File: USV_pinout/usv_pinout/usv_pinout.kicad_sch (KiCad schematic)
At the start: 3 parts

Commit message: Mostly finish, missing jetson connections
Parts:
- added LM2596_Module1, LM2596_Module2: ~, symbol vanttec_pcbs_libs:LM2596_Module
- added X8R_telemetry: ~, symbol vanttec_pcbs_libs:X8R
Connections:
- net X8R_SBUS: now reaches STM32. (ESC_1)
- net X8R_SBUS: now also X8R_telemetry. (SBUS)
- new net ?+: LM2596_Module2. (OUT+)
- new net Barrel_Jack_GND: PDB2. (+)
- new net Barrel_Jack_VIN: PDB2. (+)
- new net LM2596_1+: LM2596_Module1. (OUT+), PDB2. (+)
- new net LM2596_1-: LM2596_Module1. (OUT+), PDB2. (+)
- new net LM2596_2+: LM2596_Module2. (OUT+), PDB2. (+)
- new net LM2596_2-: LM2596_Module2. (OUT+), PDB2. (+)
- new net X8R_GND: LM2596_Module1. (OUT+), STM32. (ESC_1), X8R_telemetry. (SBUS)
- new net X8R_VIN: LM2596_Module1. (OUT+), X8R_telemetry. (SBUS)
- no-connect marks 47 -> 55
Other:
- note added: "ESC1 and ESC2 == PWM ESC7 and ESC8 == PWM"
- note added: "FrSky X8R Operating V: 4-10V"
- note added: "Step-Down Regulators (LM2596)"
- note added: "huh"
- note removed: "IMPORTANTE: Falta de conectar: - Buck Converters - No se a que vaya uno de los bucks - Radio? (O la neta no se que sea) - Las conexiones de la Jetson la neta no creo que importen"
- moved on the sheet: PDB2

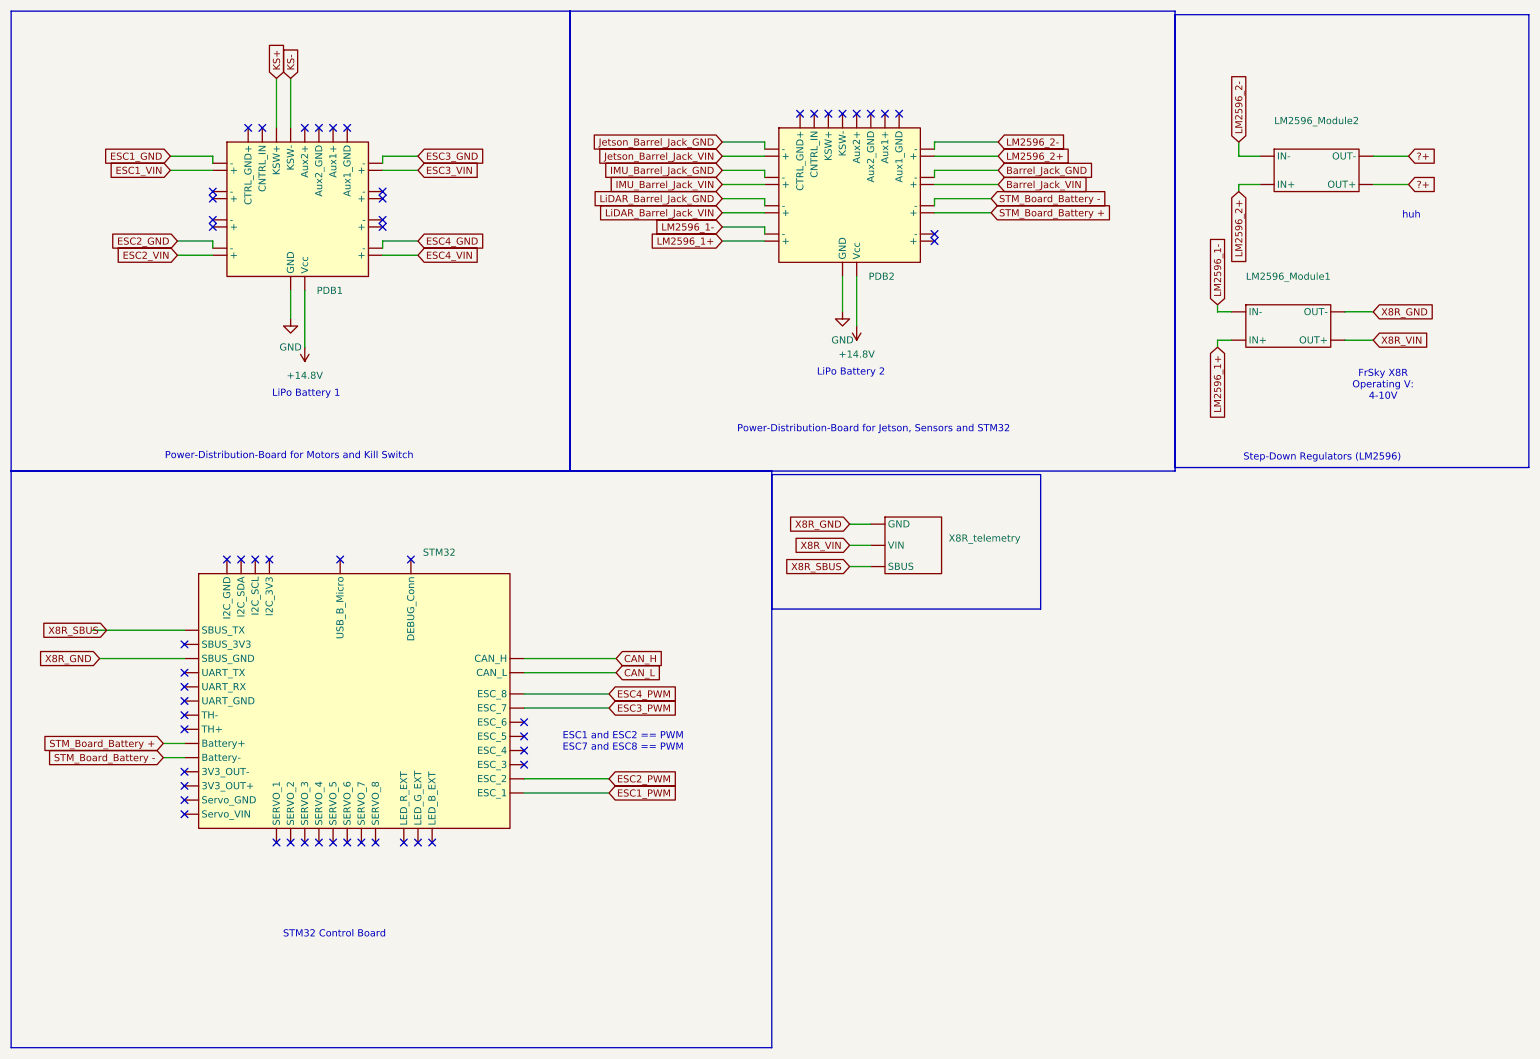
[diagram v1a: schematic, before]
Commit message: Added jetson connections
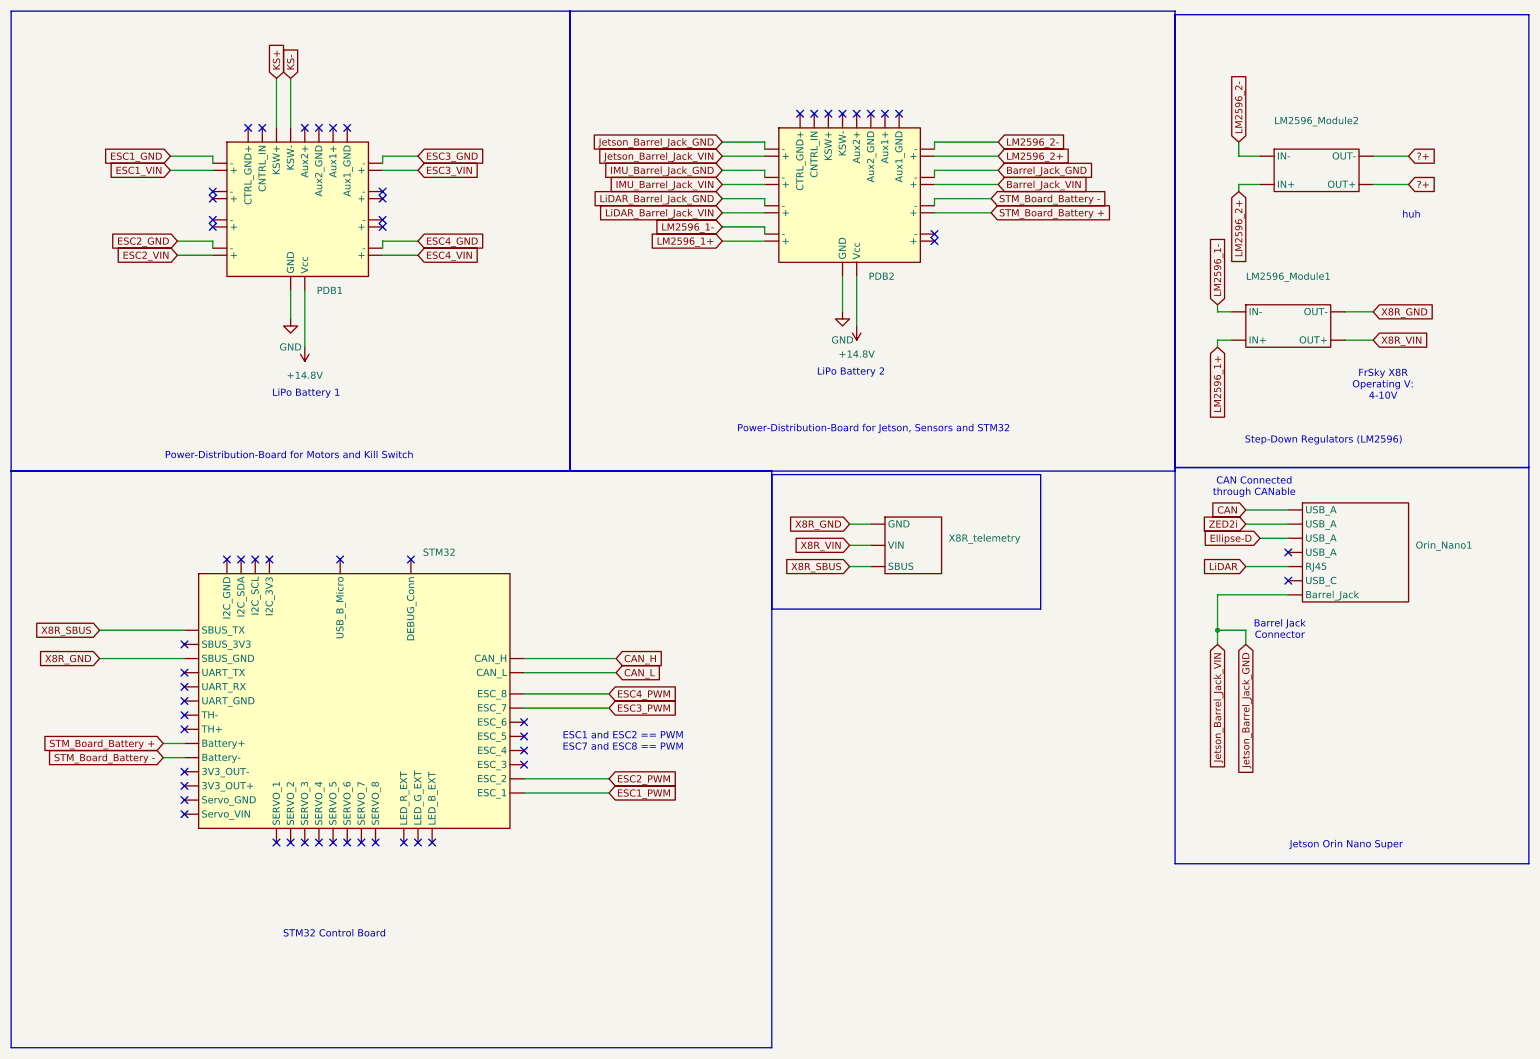
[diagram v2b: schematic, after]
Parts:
- added Orin_Nano1: ~, symbol vanttec_pcbs_libs:Orin_Nano
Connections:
- net Jetson_Barrel_Jack_VIN is gone; now on net STM_Board_Battery -: PDB2. (+)
- net Jetson_Barrel_Jack_GND: now also Orin_Nano1. (Barrel_Jack)
- new net CAN: Orin_Nano1. (Barrel_Jack)
- new net Ellipse-D: Orin_Nano1. (Barrel_Jack)
- new net LiDAR: Orin_Nano1. (Barrel_Jack)
- new net ZED2i: Orin_Nano1. (Barrel_Jack)
- no-connect marks 55 -> 57
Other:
- note added: "Barrel Jack Connector"
- note added: "CAN Connected through CANable"
- note added: "Jetson Orin Nano Super"
